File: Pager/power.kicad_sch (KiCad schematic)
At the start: 13 parts, among them J1 USB4085-GF-A_REVB, U3 MCP73831-2-OT, U4 AP2112K-3.3

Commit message: brh
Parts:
- added R6, R7: R_Small, Resistor_THT:R_Array_SIP4, symbol Device:R_Small
- added R8: 100k, Resistor_THT:R_Array_SIP4, symbol Device:R_Small
- added SW1: SW_SPDT, Package_SO:SOIC-28W_7.5x17.9mm_P1.27mm, symbol Switch:SW_SPDT
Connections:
- net GND: now also R6.2, R7.1, R8.2, SW1.3 (C)
- net V_{BATT}: now also C3.2, C6.2, U3.3 (V_{BAT}), R6.1, SW1.1 (A); no longer U4.3 (EN)
- net Charging: now reaches R2.2, U3.1 (STAT)
- new net Batt_Sense+: R7.2
- new net EN: R8.1, SW1.2 (B), U4.3 (EN)
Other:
- note added: "Charge Sensing"

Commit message: br
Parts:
- C5: value 4.7 -> 4.7uF
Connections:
- net Batt_Sense+: now also R6.2
- net GND: no longer R6.2
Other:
- moved on the sheet: R7
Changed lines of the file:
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@@
-	(wire
-		(pts
-			(xy 62.23 78.74) (xy 81.28 78.74)
-		)
-		(stroke
-			(width 0)
-			(type default)
-		)
-	)
 	(wire
 		(pts
@@
 	(wire
 		(pts
-			(xy 44.45 78.74) (xy 57.15 78.74)
+			(xy 44.45 78.74) (xy 81.28 78.74)
 		)
 		(stroke
@@
 	(wire
 		(pts
-			(xy 44.45 78.74) (xy 44.45 87.63)
+			(xy 44.45 78.74) (xy 44.45 82.55)
 		)
 		(stroke
@@
 	(symbol
 		(lib_id "Device:R_Small")
-		(at 59.69 78.74 90)
+		(at 44.45 85.09 180)
 		(unit 1)
 		(body_style 1)
@@
 		(fields_autoplaced yes)
 		(property "Reference" "R7"
-			(at 59.69 73.66 90)
+			(at 46.99 83.8199 0)
 			(show_name no)
 			(do_not_autoplace no)
@@
 					(size 1.016 1.016)
 				)
+				(justify right)
 			)
 		)
 		(property "Value" "R_Small"
-			(at 59.69 76.2 90)
-			(show_name no)
-			(do_not_autoplace no)
-			(effects
-				(font
-					(size 1.27 1.27)
-				)
+			(at 46.99 86.3599 0)
+			(show_name no)
+			(do_not_autoplace no)
+			(effects
+				(font
+					(size 1.27 1.27)
+				)
+				(justify right)
 			)
 		)
 		(property "Footprint" "Resistor_THT:R_Array_SIP4"
-			(at 59.69 78.74 0)
+			(at 44.45 85.09 0)
 			(hide yes)
 			(show_name no)
@@
 		)
 		(property "Datasheet" ""
-			(at 59.69 78.74 0)
+			(at 44.45 85.09 0)
 			(hide yes)
 			(show_name no)
@@
 		)
 		(property "Description" "Resistor, small symbol"
-			(at 59.69 78.74 0)
+			(at 44.45 85.09 0)
 			(hide yes)
 			(show_name no)
@@
 		(fields_autoplaced yes)
 		(property "Reference" "C5"
-			(at 116.84 34.2901 0)
-			(show_name no)
-			(do_not_autoplace no)
-			(effects
-				(font
-					(size 1.27 1.27)
-				)
-				(justify left)
-			)
-		)
-		(property "Value" "4.7"
-			(at 116.84 31.7501 0)
-			(show_name no)
-			(do_not_autoplace no)
-			(effects
-				(font
-					(size 1.27 1.27)
-				)
-				(justify left)
-			)
-		)
+			(at 109.22 31.7499 0)
+			(show_name no)
+			(do_not_autoplace no)
+			(effects
+				(font
+					(size 1.27 1.27)
+				)
+				(justify right)
+			)
+		)
+		(property "Value" "4.7uF"
+			(at 109.22 34.2899 0)
+			(show_name no)
+			(do_not_autoplace no)
+			(effects
+				(font
+					(size 1.27 1.27)
+				)
+				(justify right)
+			)
+		)

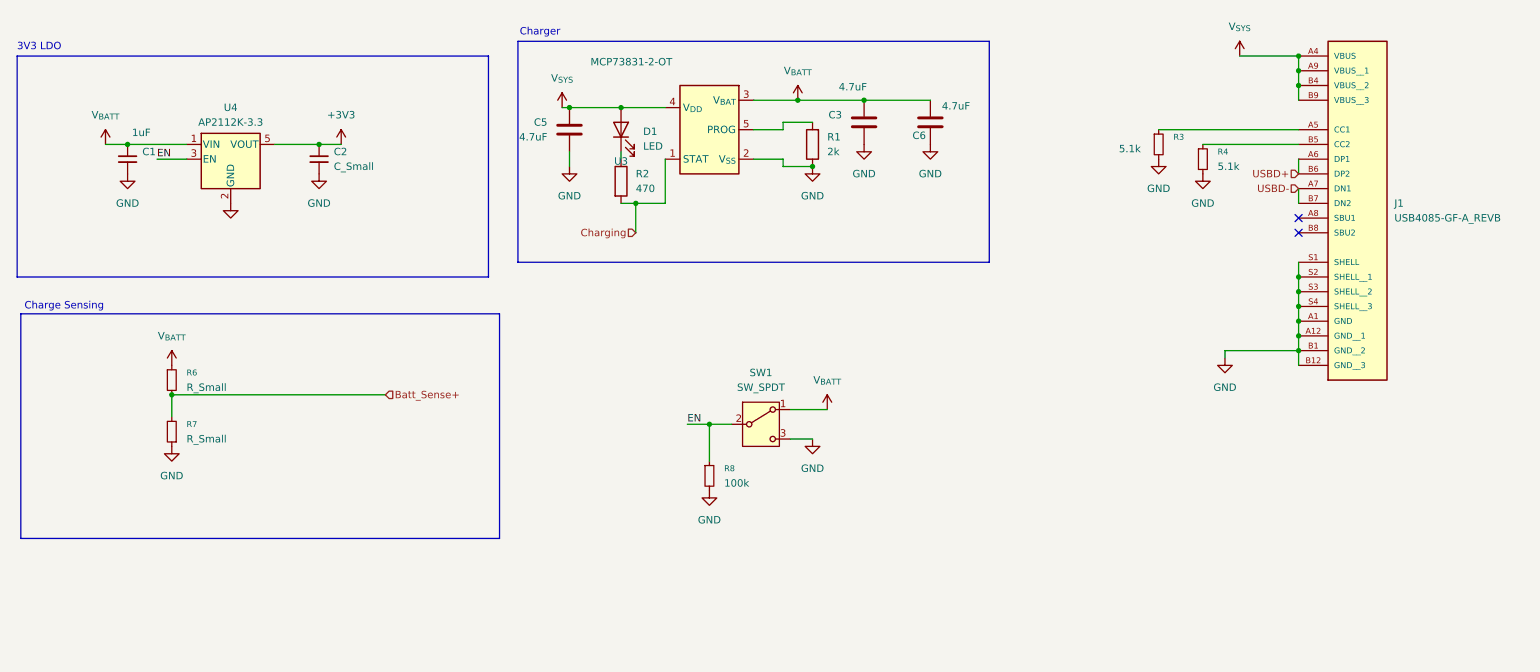
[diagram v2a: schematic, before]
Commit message: Schematic Review, Footprints Added, Need Screen
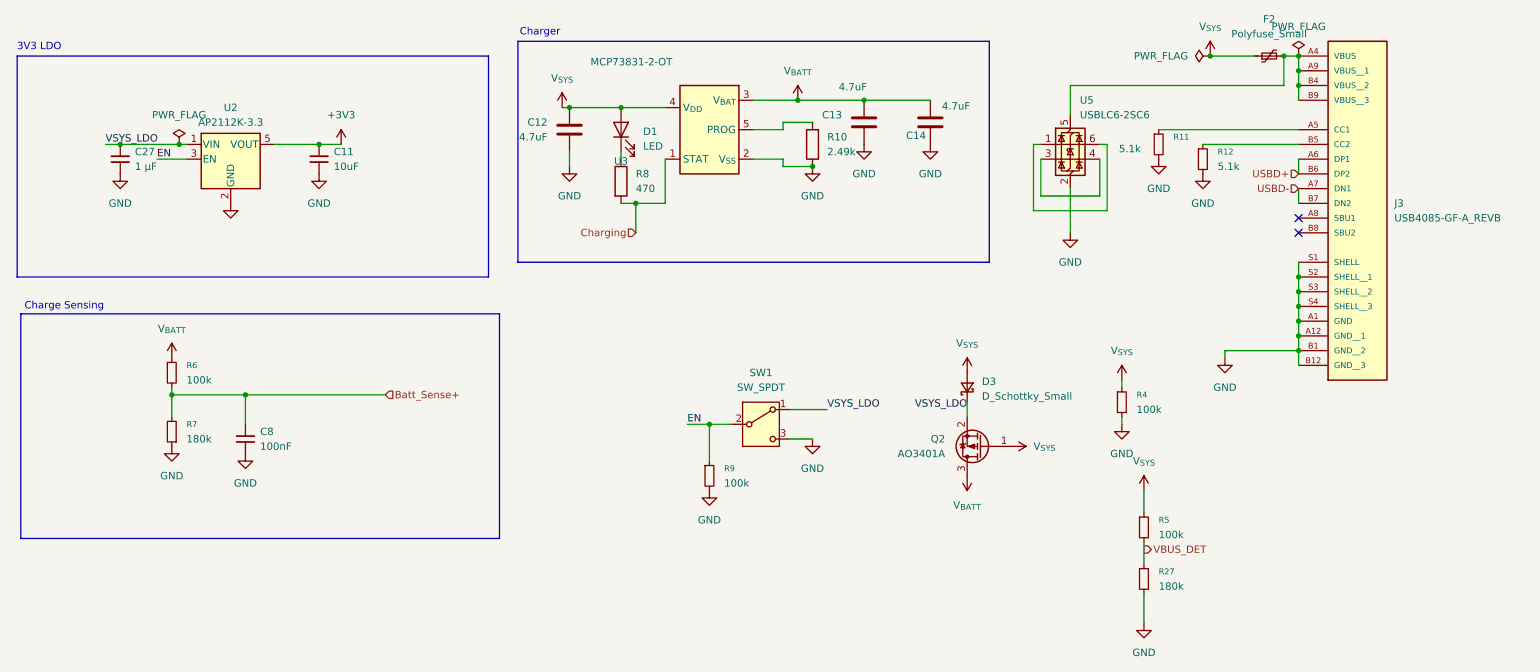
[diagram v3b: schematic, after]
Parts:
- removed C1: 1uF, symbol Device:C_Small
- added C27: 1 µF, Capacitor_SMD:C_0603_1608Metric, symbol Device:C_Small
- added C8: 100nF, Capacitor_SMD:C_0603_1608Metric, symbol Device:C_Small
- added D3: D_Schottky_Small, Diode_SMD:D_SOD-123, symbol Device:D_Schottky_Small
- added F2: Polyfuse_Small, Fuse:Fuse_1206_3216Metric, symbol Device:Polyfuse_Small
- added Q2: AO3401A, Package_TO_SOT_SMD:SOT-23, symbol Transistor_FET:AO3401A
- added R27: 180k, Resistor_SMD:R_0603_1608Metric, symbol Device:R_Small
- added R4, R5: 100k, Package_TO_SOT_SMD:SOT-23, symbol Device:R_Small
- added U5: USBLC6-2SC6, Package_TO_SOT_SMD:SOT-23-6, symbol Power_Protection:USBLC6-2SC6
- C11: renamed from C2; value C_Small -> 10uF; footprint (none) -> Capacitor_SMD:C_0603_1608Metric
- C12: renamed from C5; footprint Package_TO_SOT_SMD:SOT-23-5 -> Capacitor_SMD:C_0603_1608Metric
- C13: renamed from C3; footprint Package_TO_SOT_SMD:SOT-23-5 -> Capacitor_SMD:C_0603_1608Metric
- C14: renamed from C6; footprint Package_TO_SOT_SMD:SOT-23-5 -> Capacitor_SMD:C_0603_1608Metric
- D1: footprint (none) -> LED_SMD:LED_0603_1608Metric
- J3: renamed from J1; footprint USB4085-GF-A_REVB:GCT_USB4085-GF-A_REVB -> USB:GCT_USB4085-GF-A_REVB
- R10: renamed from R1; value 2k -> 2.49k; footprint (none) -> Package_TO_SOT_SMD:SOT-23
- R11: renamed from R3; footprint Converter_DCDC:Converter_DCDC_RECOM_R-78B-2.0_THT -> Package_TO_SOT_SMD:SOT-23
- R12: renamed from R4; footprint Converter_DCDC:Converter_DCDC_RECOM_R-78B-2.0_THT -> Package_TO_SOT_SMD:SOT-23
- R6: value R_Small -> 100k; footprint Resistor_THT:R_Array_SIP4 -> Package_TO_SOT_SMD:SOT-23
- R7: value R_Small -> 180k; footprint Resistor_THT:R_Array_SIP4 -> Package_TO_SOT_SMD:SOT-23
- R8: renamed from R2; footprint (none) -> Package_TO_SOT_SMD:SOT-23
- R9: renamed from R8; footprint Resistor_THT:R_Array_SIP4 -> Package_TO_SOT_SMD:SOT-23
- SW1: footprint Package_SO:SOIC-28W_7.5x17.9mm_P1.27mm -> Button_Switch_THT:SW_Slide_SPDT_Straight_CK_OS102011MS2Q
- renumbered U4 to U2
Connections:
- net Batt_Sense+: now also C8.2
- net GND: now also C27.2, C8.1, R27.2, R4.2, U5.2 (GND)
- net V_{BATT}: now also Q2.3 (D); no longer SW1.1 (A), U2.1 (VIN)
- net V_{SYS}: now also D3.2 (A), F2.1, Q2.1 (G), R4.1, R5.1; no longer J3.A4 (VBUS), J3.A9 (VBUS__1), J3.B4 (VBUS__2), J3.B9 (VBUS__3)
- new net: F2.2, J3.A4 (VBUS), J3.A9 (VBUS__1), J3.B4 (VBUS__2), J3.B9 (VBUS__3), U5.5 (VBUS)
- new net: U5.1 (I/O1), U5.6 (I/O1)
- new net: U5.3 (I/O2), U5.4 (I/O2)
- new net VBUS_DET: R27.1, R5.2
- new net VSYS_LDO: C27.1, D3.1 (K), Q2.2 (S), SW1.1 (A), U2.1 (VIN)
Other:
- moved on the sheet: R6

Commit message: layout
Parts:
- C11, C27, C8: footprint Capacitor_SMD:C_0603_1608Metric -> Capacitor_SMD:C_0805_2012Metric_Pad1.18x1.45mm_HandSolder
- C12, C13, C14: footprint Capacitor_SMD:C_0603_1608Metric -> Inductor_SMD:L_0805_2012Metric_Pad1.05x1.20mm_HandSolder
- J3: footprint USB:GCT_USB4085-GF-A_REVB -> Connector_USB:USB_C_Receptacle_GCT_USB4085
- R10, R11, R12, R4, R5, R6, R7, R8, R9: footprint Package_TO_SOT_SMD:SOT-23 -> Resistor_SMD:R_0805_2012Metric_Pad1.20x1.40mm_HandSolder
- R27: footprint Resistor_SMD:R_0603_1608Metric -> Resistor_SMD:R_0805_2012Metric_Pad1.20x1.40mm_HandSolder
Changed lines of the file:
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@@
 			)
 		)
-		(property "Footprint" "Capacitor_SMD:C_0603_1608Metric"
+		(property "Footprint" "Capacitor_SMD:C_0805_2012Metric_Pad1.18x1.45mm_HandSolder"
 			(at 69.85 38.1 0)
 			(hide yes)
@@
 			)
 		)
-		(property "Footprint" "Package_TO_SOT_SMD:SOT-23"
+		(property "Footprint" "Resistor_SMD:R_0805_2012Metric_Pad1.20x1.40mm_HandSolder"
 			(at 44.45 74.93 0)
 			(hide yes)
@@
 			)
 		)
-		(property "Footprint" "USB:GCT_USB4085-GF-A_REVB"
+		(property "Footprint" "Connector_USB:USB_C_Receptacle_GCT_USB4085"
 			(at 248.92 35.56 0)
 			(hide yes)
@@
 			)
 		)
-		(property "Footprint" "Capacitor_SMD:C_0603_1608Metric"
+		(property "Footprint" "Capacitor_SMD:C_0805_2012Metric_Pad1.18x1.45mm_HandSolder"
 			(at 57.15 86.36 0)
 			(hide yes)
@@
 			)
 		)
-		(property "Footprint" "Package_TO_SOT_SMD:SOT-23"
+		(property "Footprint" "Resistor_SMD:R_0805_2012Metric_Pad1.20x1.40mm_HandSolder"
 			(at 137.16 92.71 0)
 			(hide yes)
@@
 			)
 		)
-		(property "Footprint" "Package_TO_SOT_SMD:SOT-23"
+		(property "Footprint" "Resistor_SMD:R_0805_2012Metric_Pad1.20x1.40mm_HandSolder"
 			(at 156.718 35.56 90)
 			(hide yes)
@@
 			)
 		)
-		(property "Footprint" "Package_TO_SOT_SMD:SOT-23"
+		(property "Footprint" "Resistor_SMD:R_0805_2012Metric_Pad1.20x1.40mm_HandSolder"
 			(at 208.28 80.01 0)
 			(hide yes)
@@
 			)
 		)
-		(property "Footprint" "Package_TO_SOT_SMD:SOT-23"
+		(property "Footprint" "Resistor_SMD:R_0805_2012Metric_Pad1.20x1.40mm_HandSolder"
 			(at 44.45 85.09 0)
 			(hide yes)
@@
 			)
 		)
-		(property "Footprint" "Package_TO_SOT_SMD:SOT-23"
+		(property "Footprint" "Resistor_SMD:R_0805_2012Metric_Pad1.20x1.40mm_HandSolder"
 			(at 222.25 38.1 0)
 			(hide yes)
@@
 			)
 		)
-		(property "Footprint" "Package_TO_SOT_SMD:SOT-23"
+		(property "Footprint" "Resistor_SMD:R_0805_2012Metric_Pad1.20x1.40mm_HandSolder"
 			(at 120.142 41.91 90)
 			(hide yes)
@@
 			)
 		)
-		(property "Footprint" "Package_TO_SOT_SMD:SOT-23"
+		(property "Footprint" "Resistor_SMD:R_0805_2012Metric_Pad1.20x1.40mm_HandSolder"
 			(at 214.63 35.56 0)
 			(hide yes)
@@
 			)
 		)
-		(property "Footprint" "Capacitor_SMD:C_0603_1608Metric"
+		(property "Footprint" "Inductor_SMD:L_0805_2012Metric_Pad1.05x1.20mm_HandSolder"
 			(at 174.2948 27.94 0)
 			(hide yes)
@@
 			)
 		)
-		(property "Footprint" "Package_TO_SOT_SMD:SOT-23"
+		(property "Footprint" "Resistor_SMD:R_0805_2012Metric_Pad1.20x1.40mm_HandSolder"
 			(at 212.09 101.6 0)
 			(hide yes)
@@
 			)
 		)
-		(property "Footprint" "Capacitor_SMD:C_0603_1608Metric"
+		(property "Footprint" "Inductor_SMD:L_0805_2012Metric_Pad1.05x1.20mm_HandSolder"
 			(at 164.7952 27.94 0)
 			(hide yes)
@@
 			)
 		)
-		(property "Footprint" "Resistor_SMD:R_0603_1608Metric"
+		(property "Footprint" "Resistor_SMD:R_0805_2012Metric_Pad1.20x1.40mm_HandSolder"
 			(at 212.09 110.49 0)
 			(hide yes)
@@
 		(in_pos_files yes)
 		(dnp no)
-		(fields_autoplaced yes)
 		(property "Reference" "C27"
-			(at 38.1 36.8299 0)
+			(at 36.322 40.64 0)
 			(show_name no)
 			(do_not_autoplace no)
@@
 		)
 		(property "Value" "1 µF"
-			(at 38.1 39.3699 0)
+			(at 28.448 39.37 0)
 			(show_name no)
 			(do_not_autoplace no)
@@
 			)
 		)
-		(property "Footprint" "Capacitor_SMD:C_0603_1608Metric"
+		(property "Footprint" "Capacitor_SMD:C_0805_2012Metric_Pad1.18x1.45mm_HandSolder"
 			(at 35.56 38.1 0)
 			(hide yes)
@@
 			)
 		)
-		(property "Footprint" "Capacitor_SMD:C_0603_1608Metric"
+		(property "Footprint" "Inductor_SMD:L_0805_2012Metric_Pad1.05x1.20mm_HandSolder"
 			(at 113.9952 29.21 0)
 			(hide yes)

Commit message: power
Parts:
- removed D3: D_Schottky_Small, Diode_SMD:D_SOD-123, symbol Device:D_Schottky_Small
- removed Q2: AO3401A, Package_TO_SOT_SMD:SOT-23, symbol Transistor_FET:AO3401A
- removed R27: 180k, Resistor_SMD:R_0805_2012Metric_Pad1.20x1.40mm_HandSolder, symbol Device:R_Small
- removed R4, R5: 100k, Resistor_SMD:R_0805_2012Metric_Pad1.20x1.40mm_HandSolder, symbol Device:R_Small
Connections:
- net VSYS_LDO renamed V_{LDO}
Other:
- moved on the sheet: R9, SW1

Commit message: esp32
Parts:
- added R27: 180k, Resistor_SMD:R_0805_2012Metric_Pad1.20x1.40mm_HandSolder, symbol Device:R_Small
- added R4, R5: 100k, Resistor_SMD:R_0805_2012Metric_Pad1.20x1.40mm_HandSolder, symbol Device:R_Small
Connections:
- net GND: now also R27.2, R4.2
- net V_{SYS}: now also R4.1, R5.1
- new net: R27.1, R5.2
